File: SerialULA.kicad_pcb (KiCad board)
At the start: 2 copper layers, 17.8 x 35.6 mm, 17 parts, among them J1 JTAG-IDC, U1 XC9572XL-10VQG44C, U2 AMS1117-3.3, U3 2C199

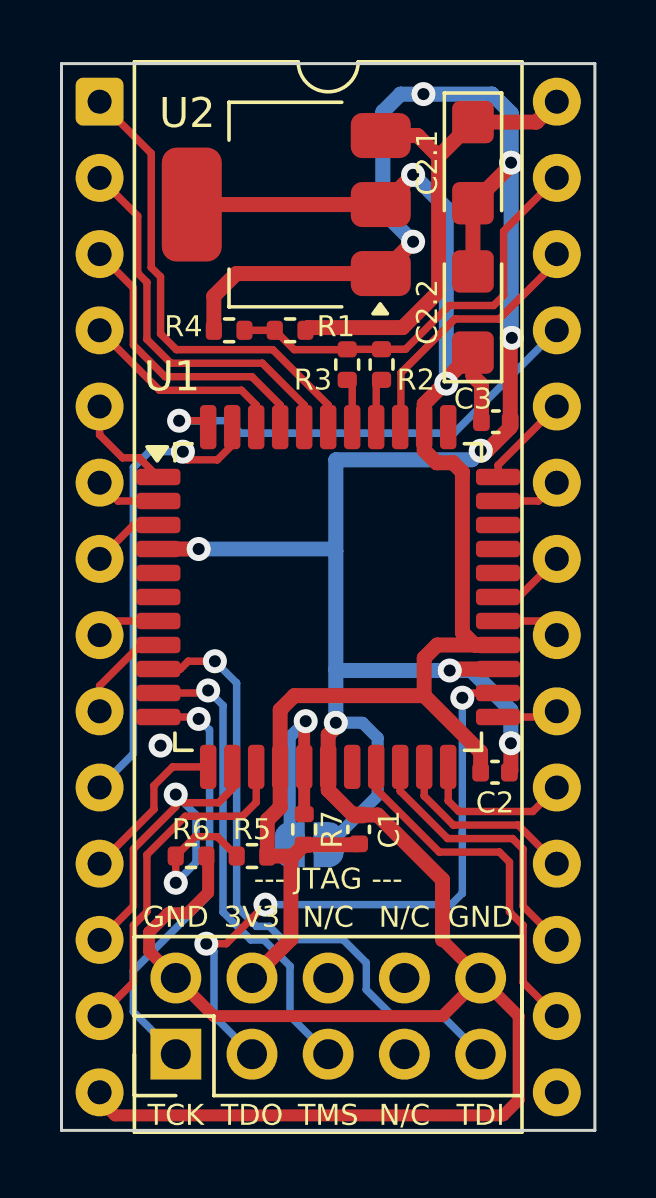
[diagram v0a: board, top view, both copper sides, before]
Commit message: Initial commit of Rev 02 hardware
- Dual footprint for both large and small LDO regulator / capacitors.
- Updated resistor values at R1, R2, R3 & R4 for CasOutX. Now pulling up to 3.3V instead of 5V
- Connected extra solder bridge with pull up into spare CPLD input for possible future 'extended features'.
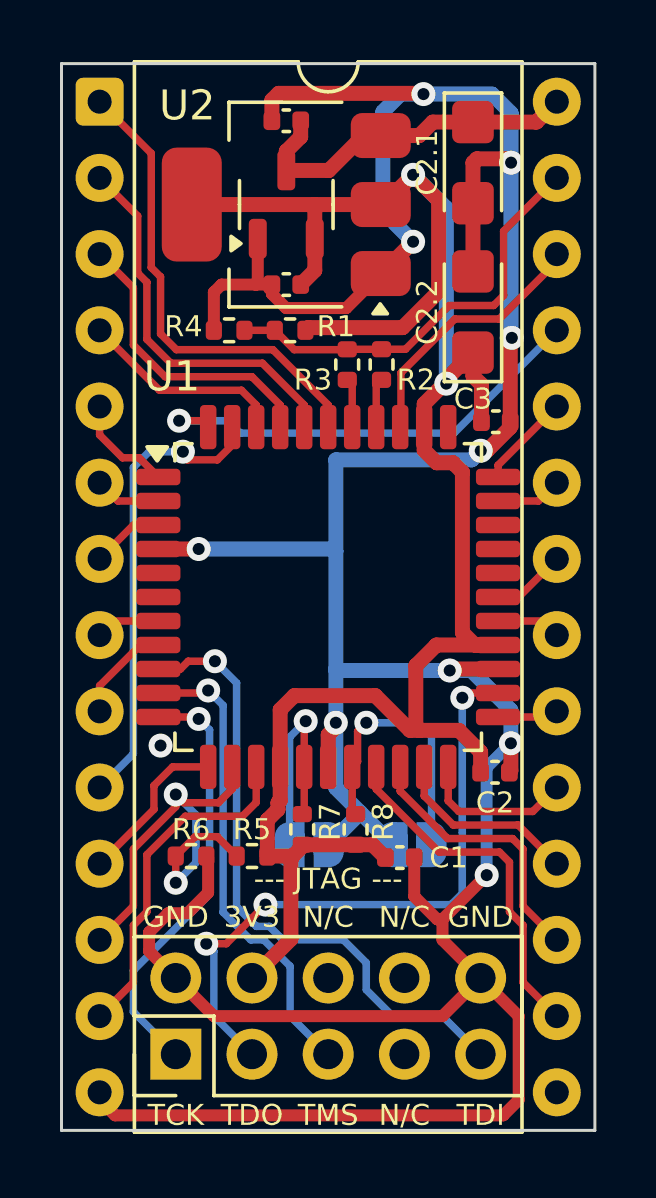
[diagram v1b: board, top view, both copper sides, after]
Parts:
- added C4: 1u, Capacitor_SMD:C_0402_1005Metric, F.Cu at (84.2, 40.5)
- added C5: 1u, Capacitor_SMD:C_0402_1005Metric, F.Cu at (84.2, 46.0)
- added JP2: SolderJumper_2_Open, Jumper:SolderJumper-2_P1.3mm_Open_RoundedPad1.0x1.5mm, B.Cu at (88.4, 64.6)
- added R8: 10K, Resistor_SMD:R_0402_1005Metric, F.Cu at (86.5, 64.1)
- added U3: XC6206P332MR, Package_TO_SOT_SMD:SOT-23-3, F.Cu at (84.2, 43.3)
- R1: value 1K0 -> 2K0
- R3: value 10K -> 1K0
- R4: value 47K -> 2K0
- moved C1 1.66 mm to (88.0, 65.1), turned to 0 degrees
- moved R7 0.06 mm to (84.7, 64.1)
- renumbered U3 to U4
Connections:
- R1 pad 1: +5V -> +3.3V
- U1 pad 18: unconnected-(U1-P18-Pad18) -> Net-(JP2-B)
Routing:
- net +3.3V: track 55.7 -> 70.8 mm
- net GND: track 117.9 -> 129.8 mm, vias 10 -> 11
- net Net-(JP2-B): track 0.00 -> 9.26 mm, vias 0 -> 1
- net +5V: track 16.4 -> 12.5 mm
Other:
- board text added: "Rev 02"
- board text added: "© Ken Lowe & David Banks June 2025"
- board text removed: "Rev 01"
- board text removed: "© Ken Lowe & David Banks May 2025"
